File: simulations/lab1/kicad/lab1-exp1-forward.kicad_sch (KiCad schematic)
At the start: 5 parts

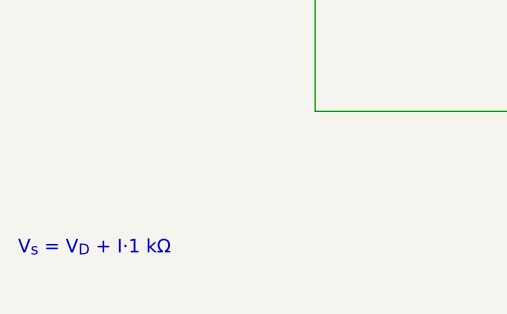
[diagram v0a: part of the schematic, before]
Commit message: feat(kicad): 五張 Lab 1 原理圖加入 ngspice 模擬指令，可在 KiCad 內建模擬器直接跑
- **新增** `gen_exp1`～`gen_exp4_rc` 各放一行 `.dc`／`.tran` 指令文字，重新產生原理圖、SPICE 網表、SVG 與 PDF，ERC 仍為 0 錯誤
- **調整** `kicad/README.md` 說明 GUI 模擬步驟與 `kicad-cli` 沒有 `sim` 子命令的限制
- **調整** 筆記用的 `public/note-images/ec-week3-kicad/` 五張圖同步

Co-Authored-By: Claude Fable 5.1 <noreply@anthropic.com>
Claude-Session: https://claude.ai/code/session_01CSTJPweMCqSNGPRV9i9S1L
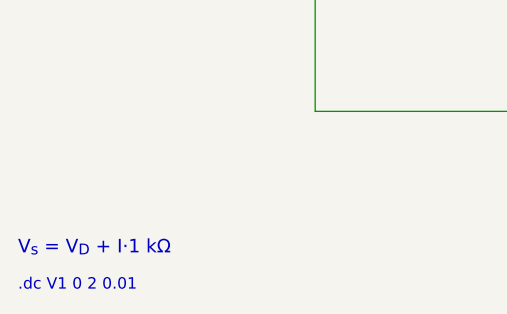
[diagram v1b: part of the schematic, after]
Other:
- note added: ".dc V1 0 2 0.01"
